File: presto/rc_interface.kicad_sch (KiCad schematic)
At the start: 0 parts

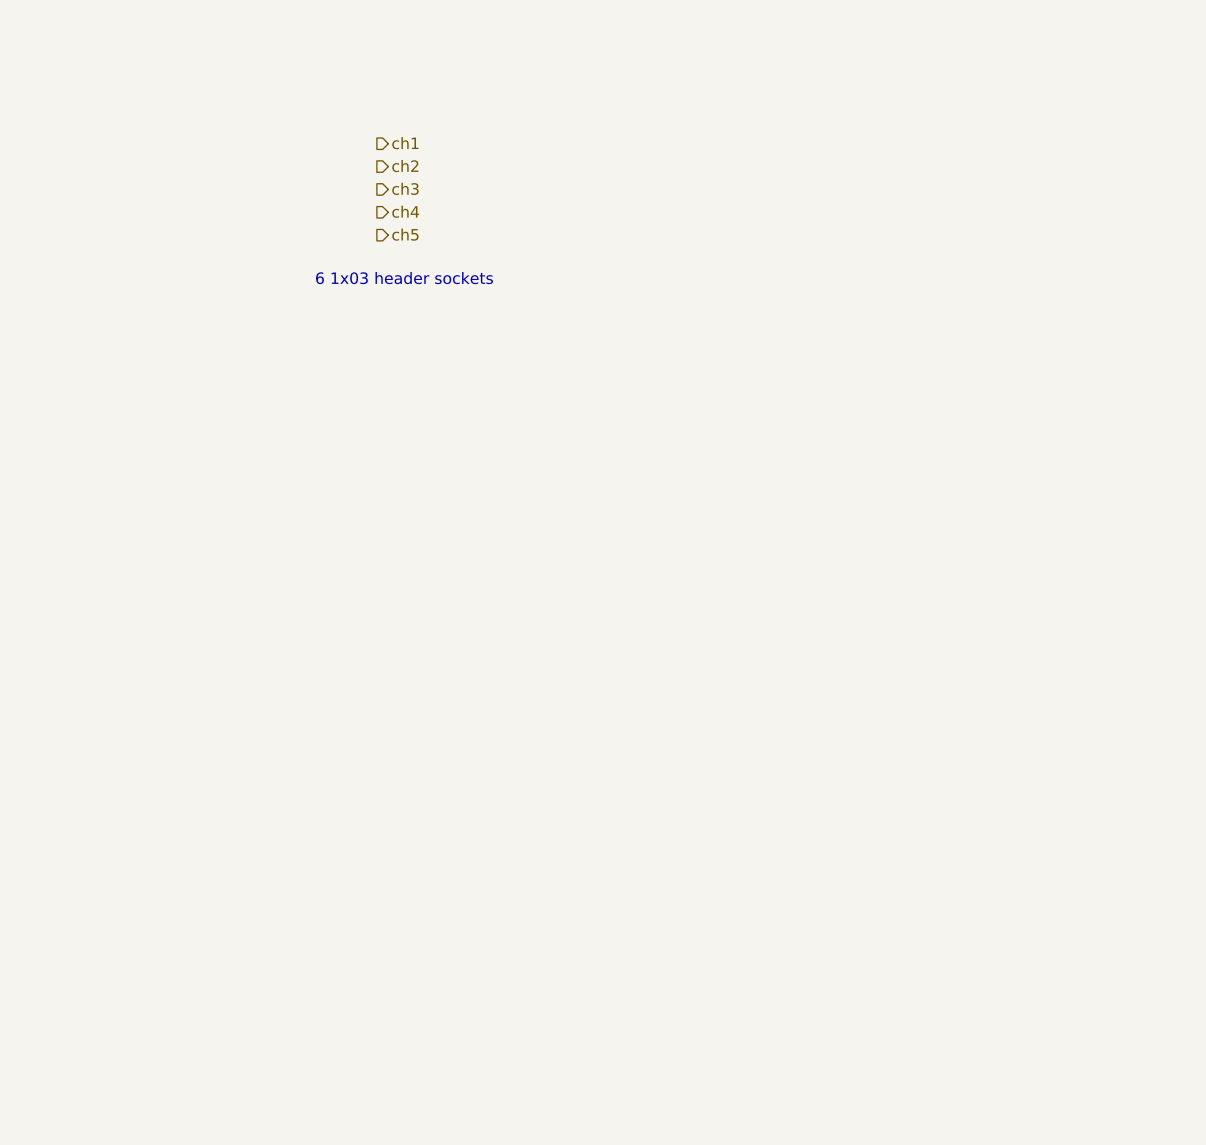
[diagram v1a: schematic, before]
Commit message: RC and Servo interface schematic done
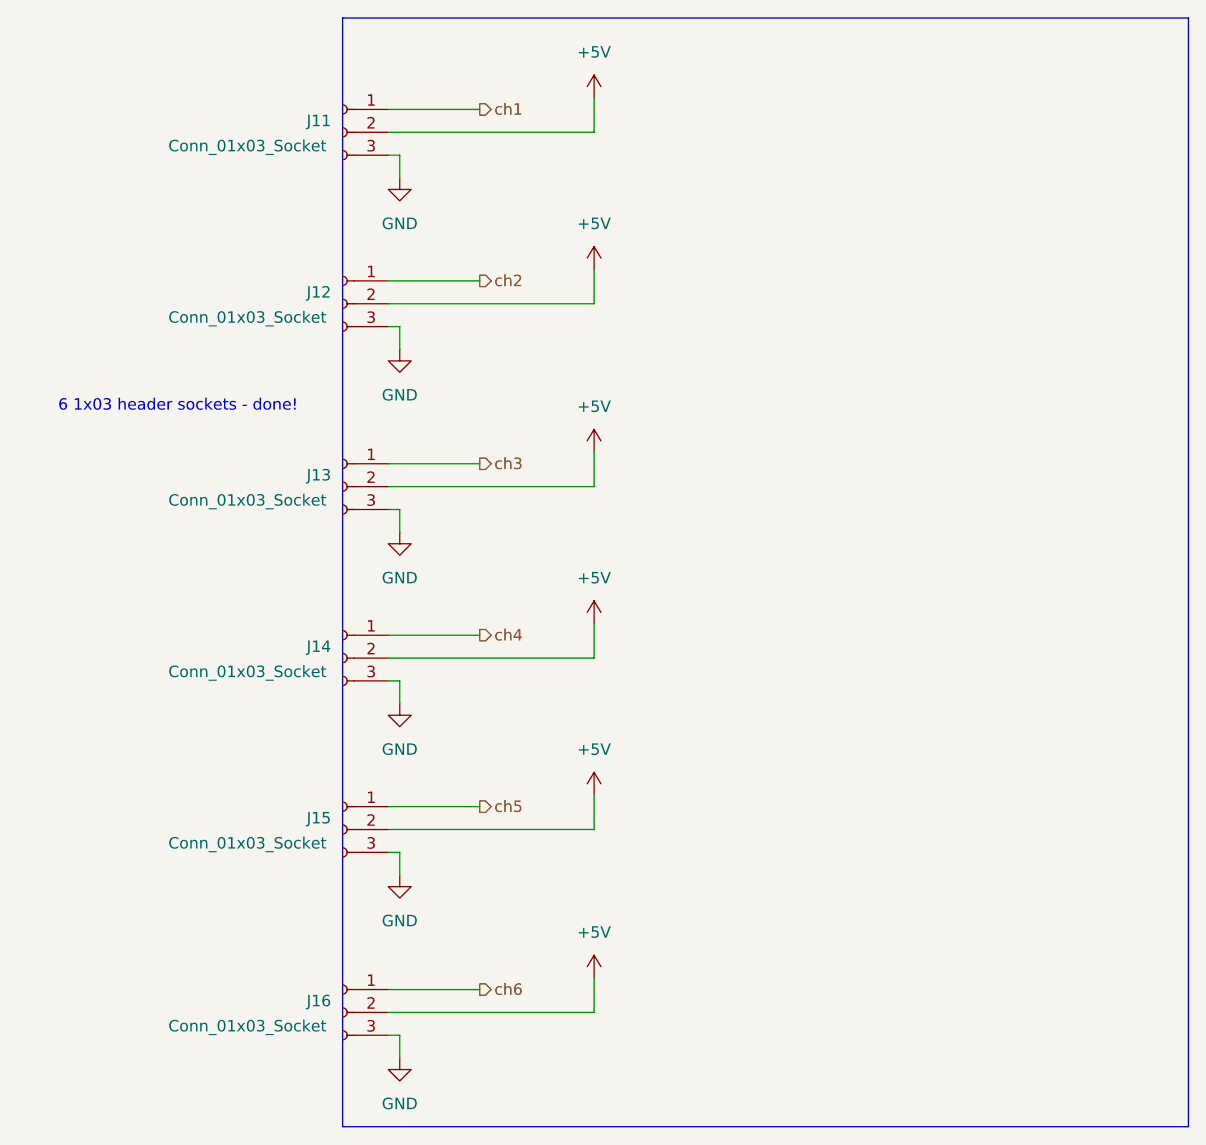
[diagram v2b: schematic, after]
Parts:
- added J11, J12, J13, J14, J15, J16: Conn_01x03_Socket, Connector_PinSocket_2.54mm:PinSocket_1x03_P2.54mm_Vertical, symbol Connector:Conn_01x03_Socket
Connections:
- net ch1: now also J11.1 (Pin_1)
- net ch2: now also J12.1 (Pin_1)
- net ch3: now also J13.1 (Pin_1)
- net ch4: now also J14.1 (Pin_1)
- net ch5: now also J15.1 (Pin_1)
- new net +5V: J11.2 (Pin_2), J12.2 (Pin_2), J13.2 (Pin_2), J14.2 (Pin_2), J15.2 (Pin_2), J16.2 (Pin_2)
- new net GND: J11.3 (Pin_3), J12.3 (Pin_3), J13.3 (Pin_3), J14.3 (Pin_3), J15.3 (Pin_3), J16.3 (Pin_3)
- new net ch6: J16.1 (Pin_1)
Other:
- note added: "6 1x03 header sockets - done!"
- note removed: "6 1x03 header sockets"

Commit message: Presto PCB edited with schematic, components placed, wiring in progress
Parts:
- renumbered J11 to J501, J12 to J502, J13 to J503, J14 to J504, J15 to J505, J16 to J506
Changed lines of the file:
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@@
 		(dnp no)
 		(fields_autoplaced yes)
-		(property "Reference" "#PWR022"
+		(property "Reference" "#PWR0501"
 			(at 119.38 63.5 0)
 			(effects
@@
 			(project ""
 				(path "/0fac30c0-3f82-4ab4-8888-b9c60b2e0ca9/7c259685-6390-4991-b1d4-6a2dc1de7b36"
-					(reference "#PWR022")
+					(reference "#PWR0501")
 					(unit 1)
 				)
@@
 		(dnp no)
 		(fields_autoplaced yes)
-		(property "Reference" "#PWR021"
+		(property "Reference" "#PWR0507"
 			(at 140.97 52.07 0)
 			(effects
@@
 			(project "presto"
 				(path "/0fac30c0-3f82-4ab4-8888-b9c60b2e0ca9/7c259685-6390-4991-b1d4-6a2dc1de7b36"
-					(reference "#PWR021")
+					(reference "#PWR0507")
 					(unit 1)
 				)
@@
 		(on_board yes)
 		(dnp no)
-		(property "Reference" "J16"
+		(property "Reference" "J506"
 			(at 111.76 148.5899 0)
 			(effects
@@
 			(project "presto"
 				(path "/0fac30c0-3f82-4ab4-8888-b9c60b2e0ca9/7c259685-6390-4991-b1d4-6a2dc1de7b36"
-					(reference "J16")
+					(reference "J506")
 					(unit 1)
 				)
@@
 		(dnp no)
 		(fields_autoplaced yes)
-		(property "Reference" "#PWR025"
+		(property "Reference" "#PWR0503"
 			(at 119.38 102.87 0)
 			(effects
@@
 			(project "presto"
 				(path "/0fac30c0-3f82-4ab4-8888-b9c60b2e0ca9/7c259685-6390-4991-b1d4-6a2dc1de7b36"
-					(reference "#PWR025")
+					(reference "#PWR0503")
 					(unit 1)
 				)
@@
 		(on_board yes)
 		(dnp no)
-		(property "Reference" "J15"
+		(property "Reference" "J505"
 			(at 111.76 128.2699 0)
 			(effects
@@
 			(project "presto"
 				(path "/0fac30c0-3f82-4ab4-8888-b9c60b2e0ca9/7c259685-6390-4991-b1d4-6a2dc1de7b36"
-					(reference "J15")
+					(reference "J505")
 					(unit 1)
 				)
@@
 		(dnp no)
 		(fields_autoplaced yes)
-		(property "Reference" "#PWR031"
+		(property "Reference" "#PWR0506"
 			(at 119.38 161.29 0)
 			(effects
@@
 			(project "presto"
 				(path "/0fac30c0-3f82-4ab4-8888-b9c60b2e0ca9/7c259685-6390-4991-b1d4-6a2dc1de7b36"
-					(reference "#PWR031")
+					(reference "#PWR0506")
 					(unit 1)
 				)
@@
 		(dnp no)
 		(fields_autoplaced yes)
-		(property "Reference" "#PWR024"
+		(property "Reference" "#PWR0508"
 			(at 140.97 71.12 0)
 			(effects
@@
 			(project "presto"
 				(path "/0fac30c0-3f82-4ab4-8888-b9c60b2e0ca9/7c259685-6390-4991-b1d4-6a2dc1de7b36"
-					(reference "#PWR024")
+					(reference "#PWR0508")
 					(unit 1)
 				)
@@
 		(dnp no)
 		(fields_autoplaced yes)
-		(property "Reference" "#PWR026"
+		(property "Reference" "#PWR0509"
 			(at 140.97 91.44 0)
 			(effects
@@
 			(project "presto"
 				(path "/0fac30c0-3f82-4ab4-8888-b9c60b2e0ca9/7c259685-6390-4991-b1d4-6a2dc1de7b36"
-					(reference "#PWR026")
+					(reference "#PWR0509")
 					(unit 1)
 				)
@@
 		(on_board yes)
 		(dnp no)
-		(property "Reference" "J13"
+		(property "Reference" "J503"
 			(at 111.76 90.1699 0)
 			(effects
@@
 			(project "presto"
 				(path "/0fac30c0-3f82-4ab4-8888-b9c60b2e0ca9/7c259685-6390-4991-b1d4-6a2dc1de7b36"
-					(reference "J13")
+					(reference "J503")
 					(unit 1)
 				)
@@
 		(on_board yes)
 		(dnp no)
-		(property "Reference" "J14"
+		(property "Reference" "J504"
 			(at 111.76 109.2199 0)
 			(effects
@@
 			(project "presto"
 				(path "/0fac30c0-3f82-4ab4-8888-b9c60b2e0ca9/7c259685-6390-4991-b1d4-6a2dc1de7b36"
-					(reference "J14")
+					(reference "J504")
 					(unit 1)
 				)
@@
 		(dnp no)
 		(fields_autoplaced yes)
-		(property "Reference" "#PWR028"
+		(property "Reference" "#PWR0510"
 			(at 140.97 110.49 0)
 			(effects
@@
 			(project "presto"
 				(path "/0fac30c0-3f82-4ab4-8888-b9c60b2e0ca9/7c259685-6390-4991-b1d4-6a2dc1de7b36"
-					(reference "#PWR028")
+					(reference "#PWR0510")
 					(unit 1)
 				)
@@
 		(dnp no)
 		(fields_autoplaced yes)
-		(property "Reference" "#PWR030"
+		(property "Reference" "#PWR0511"
 			(at 140.97 129.54 0)
 			(effects
@@
 			(project "presto"
 				(path "/0fac30c0-3f82-4ab4-8888-b9c60b2e0ca9/7c259685-6390-4991-b1d4-6a2dc1de7b36"
-					(reference "#PWR030")
+					(reference "#PWR0511")
 					(unit 1)
 				)
@@
 		(dnp no)
 		(fields_autoplaced yes)
-		(property "Reference" "#PWR027"
+		(property "Reference" "#PWR0504"
 			(at 119.38 121.92 0)
 			(effects
@@
 			(project "presto"
 				(path "/0fac30c0-3f82-4ab4-8888-b9c60b2e0ca9/7c259685-6390-4991-b1d4-6a2dc1de7b36"
-					(reference "#PWR027")
+					(reference "#PWR0504")
 					(unit 1)
 				)
@@
 		(on_board yes)
 		(dnp no)
-		(property "Reference" "J12"
+		(property "Reference" "J502"
 			(at 111.76 69.8499 0)
 			(effects
@@
 			(project "presto"
 				(path "/0fac30c0-3f82-4ab4-8888-b9c60b2e0ca9/7c259685-6390-4991-b1d4-6a2dc1de7b36"
-					(reference "J12")
+					(reference "J502")
 					(unit 1)
 				)
@@
 		(dnp no)
 		(fields_autoplaced yes)
-		(property "Reference" "#PWR023"
+		(property "Reference" "#PWR0502"
 			(at 119.38 82.55 0)
 			(effects
@@
 			(project "presto"
 				(path "/0fac30c0-3f82-4ab4-8888-b9c60b2e0ca9/7c259685-6390-4991-b1d4-6a2dc1de7b36"
-					(reference "#PWR023")
+					(reference "#PWR0502")
 					(unit 1)
 				)
@@
 		(on_board yes)
 		(dnp no)
-		(property "Reference" "J11"
+		(property "Reference" "J501"
 			(at 111.76 50.7999 0)
 			(effects
@@
 			(project ""
 				(path "/0fac30c0-3f82-4ab4-8888-b9c60b2e0ca9/7c259685-6390-4991-b1d4-6a2dc1de7b36"
-					(reference "J11")
+					(reference "J501")
 					(unit 1)
 				)
@@
 		(dnp no)
 		(fields_autoplaced yes)
-		(property "Reference" "#PWR032"
+		(property "Reference" "#PWR0512"
 			(at 140.97 149.86 0)
 			(effects
@@
 			(project "presto"
 				(path "/0fac30c0-3f82-4ab4-8888-b9c60b2e0ca9/7c259685-6390-4991-b1d4-6a2dc1de7b36"
-					(reference "#PWR032")
+					(reference "#PWR0512")
 					(unit 1)
 				)
@@
 		(dnp no)
 		(fields_autoplaced yes)
-		(property "Reference" "#PWR029"
+		(property "Reference" "#PWR0505"
 			(at 119.38 140.97 0)
 			(effects
@@
 			(project "presto"
 				(path "/0fac30c0-3f82-4ab4-8888-b9c60b2e0ca9/7c259685-6390-4991-b1d4-6a2dc1de7b36"
-					(reference "#PWR029")
-					(unit 1)
-				)
+					(reference "#PWR0505")
+					(unit 1)
+				)
